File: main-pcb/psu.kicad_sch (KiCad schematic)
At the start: 124 parts, among them J1 CONN_01X03, J2 CORTEX_DEBUG_ETM, SW1 SWITCH, SW2 SWITCH, U10 NCP45525IMNTWG-H, U11 LTC3374-QFN, U19 INA230, U2 STM32L431-QFN48, U3 INA230, U4 INA230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

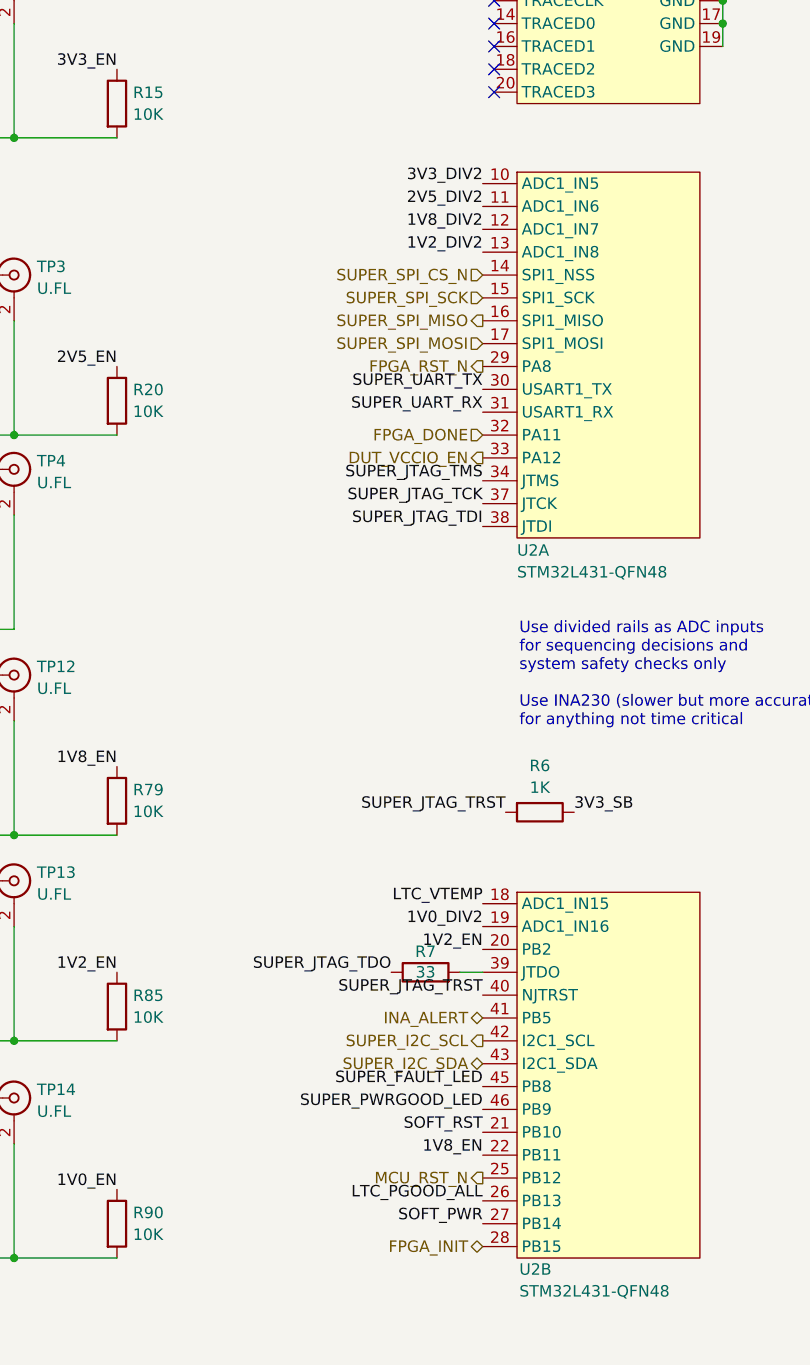
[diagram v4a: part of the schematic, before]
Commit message: Continued routing power supply
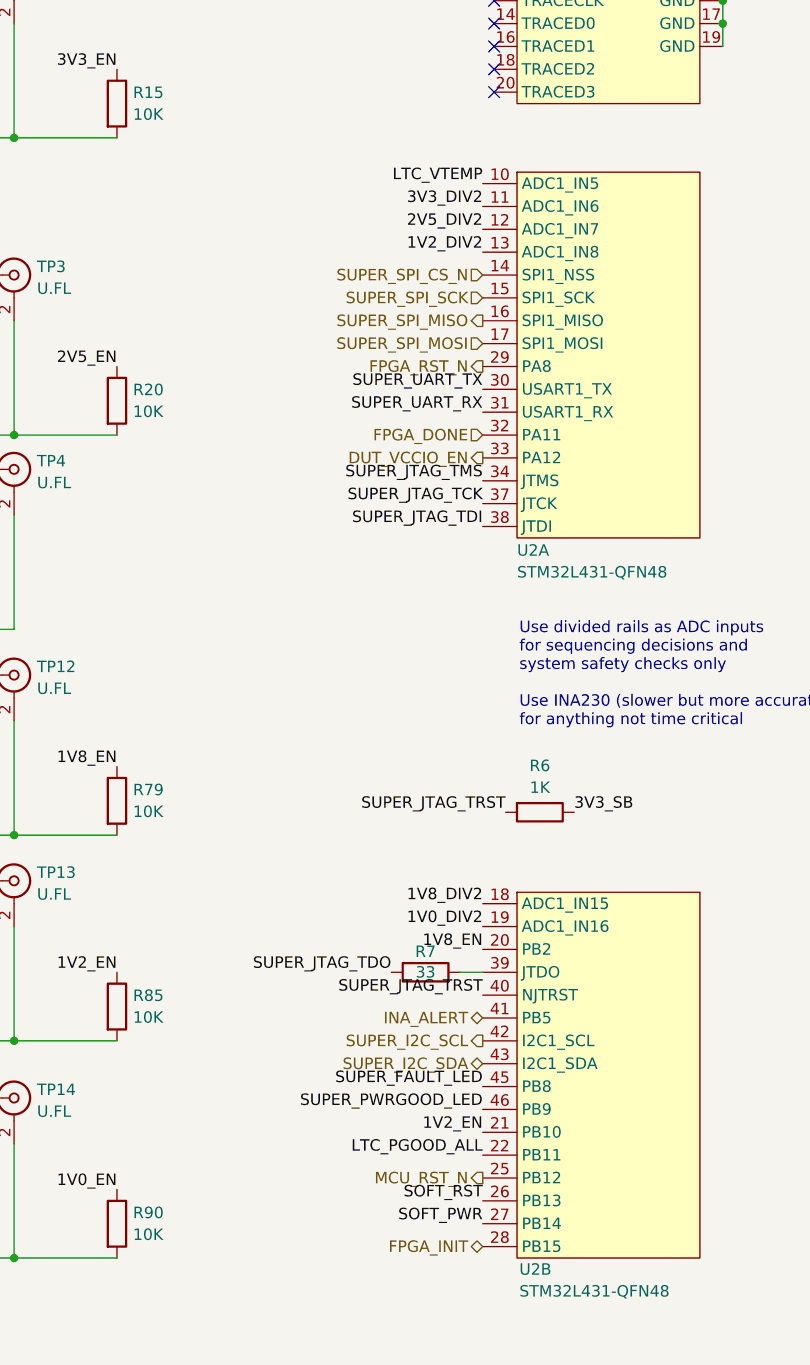
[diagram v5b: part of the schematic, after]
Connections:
- net 1V2_EN: now also U2.21 (PB10); no longer U2.20 (PB2)
- net 1V8_DIV2: now also U2.18 (PB0); no longer U2.12 (PA2)
- net 1V8_EN: now also U2.20 (PB2); no longer U2.22 (PB11)
- net 2V5_DIV2: now also U2.12 (PA2); no longer U2.11 (PA1)
- net 3V3_DIV2: now also U2.11 (PA1); no longer U2.10 (PA0)
- net LTC_PGOOD_ALL: now also U2.22 (PB11); no longer U2.26 (PB13)
- net LTC_VTEMP: now also U2.10 (PA0); no longer U2.18 (PB0)
- net SOFT_RST: now also U2.26 (PB13); no longer U2.21 (PB10)
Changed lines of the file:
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@@
 	)
 	(label "1V2_EN"
-		(at 255.27 148.59 180)
+		(at 255.27 168.91 180)
 		(fields_autoplaced yes)
 		(effects
@@
 	)
 	(label "SOFT_RST"
-		(at 255.27 168.91 180)
+		(at 255.27 176.53 180)
 		(fields_autoplaced yes)
 		(effects
@@
 	)
 	(label "1V8_DIV2"
-		(at 255.27 68.58 180)
+		(at 255.27 143.51 180)
 		(fields_autoplaced yes)
 		(effects
@@
 	)
 	(label "LTC_VTEMP"
-		(at 255.27 143.51 180)
+		(at 255.27 63.5 180)
 		(fields_autoplaced yes)
 		(effects
@@
 	)
 	(label "3V3_DIV2"
-		(at 255.27 63.5 180)
+		(at 255.27 66.04 180)
 		(fields_autoplaced yes)
 		(effects
@@
 	)
 	(label "1V8_EN"
-		(at 255.27 171.45 180)
+		(at 255.27 148.59 180)
 		(fields_autoplaced yes)
 		(effects
@@
 	)
 	(label "LTC_PGOOD_ALL"
-		(at 255.27 176.53 180)
+		(at 255.27 171.45 180)
 		(fields_autoplaced yes)
 		(effects
@@
 	)
 	(label "2V5_DIV2"
-		(at 255.27 66.04 180)
-		(fields_autoplaced yes)
-		(effects
+		(at 255.27 68.58 180)
+		(fields_autoplaced yes)
+		(effects

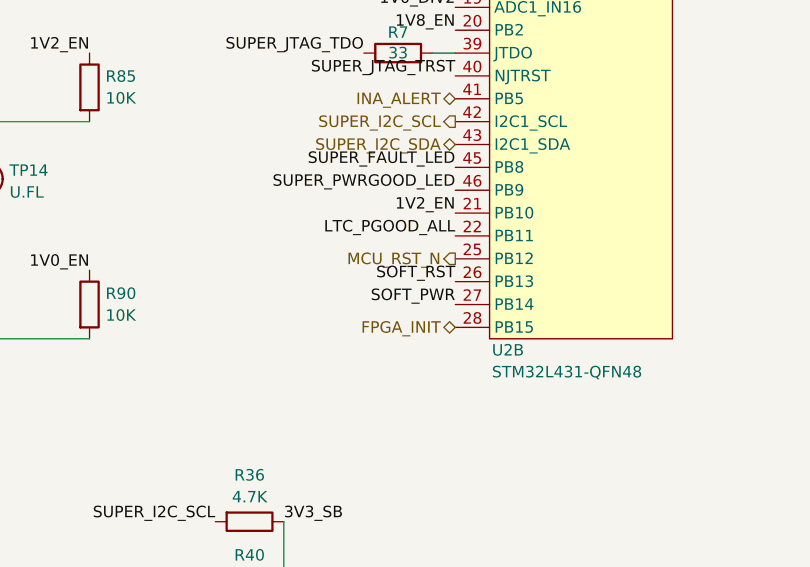
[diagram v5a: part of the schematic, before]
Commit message: Continued layout, added first ground plane layer. 26 nets unrouted, still need to place last two INA230s
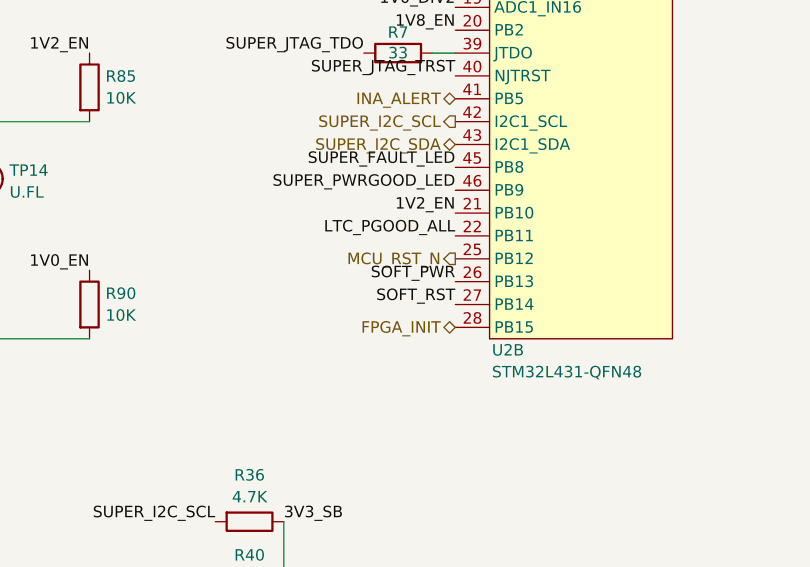
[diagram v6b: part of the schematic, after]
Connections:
- net SOFT_PWR: now also U2.26 (PB13); no longer U2.27 (PB14)
- net SOFT_RST: now also U2.27 (PB14); no longer U2.26 (PB13)
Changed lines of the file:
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@@
 	(title_block
 		(title "DUMPTRUCK flash dumper")
-		(date "2024-10-20")
+		(date "2024-10-23")
 		(rev "0.1")
 		(company "Antikernel Labs")
@@
 	)
 	(label "SOFT_RST"
-		(at 255.27 176.53 180)
+		(at 255.27 179.07 180)
 		(fields_autoplaced yes)
 		(effects
@@
 	)
 	(label "SOFT_PWR"
-		(at 255.27 179.07 180)
+		(at 255.27 176.53 180)
 		(fields_autoplaced yes)
 		(effects
